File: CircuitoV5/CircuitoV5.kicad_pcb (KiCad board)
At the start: 2 copper layers, 27 x 62 mm, 18 parts, among them J1 Conn_01x05, J2 Screw_Terminal_01x02, J3 Screw_Terminal_01x02, U1 LM324, U2 LM358

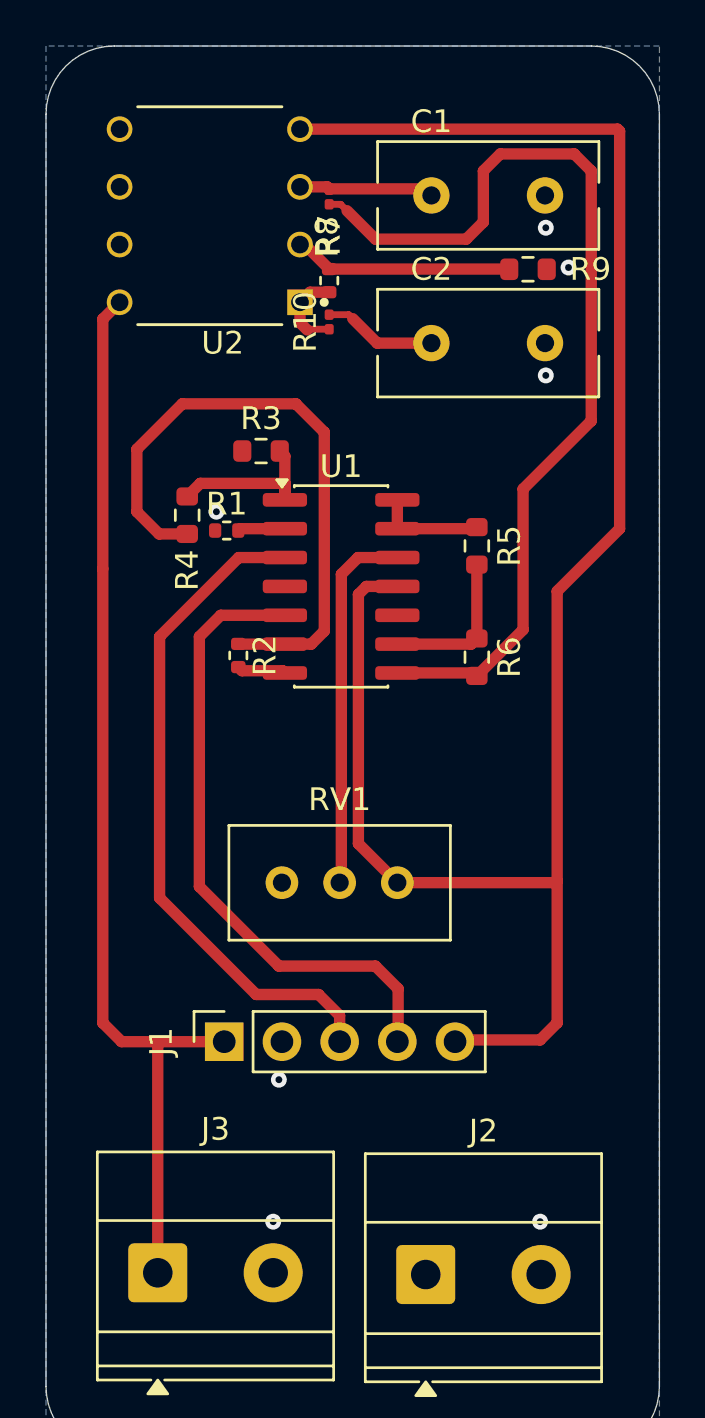
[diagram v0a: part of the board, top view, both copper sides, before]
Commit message: Enrutamiento v2 parcial
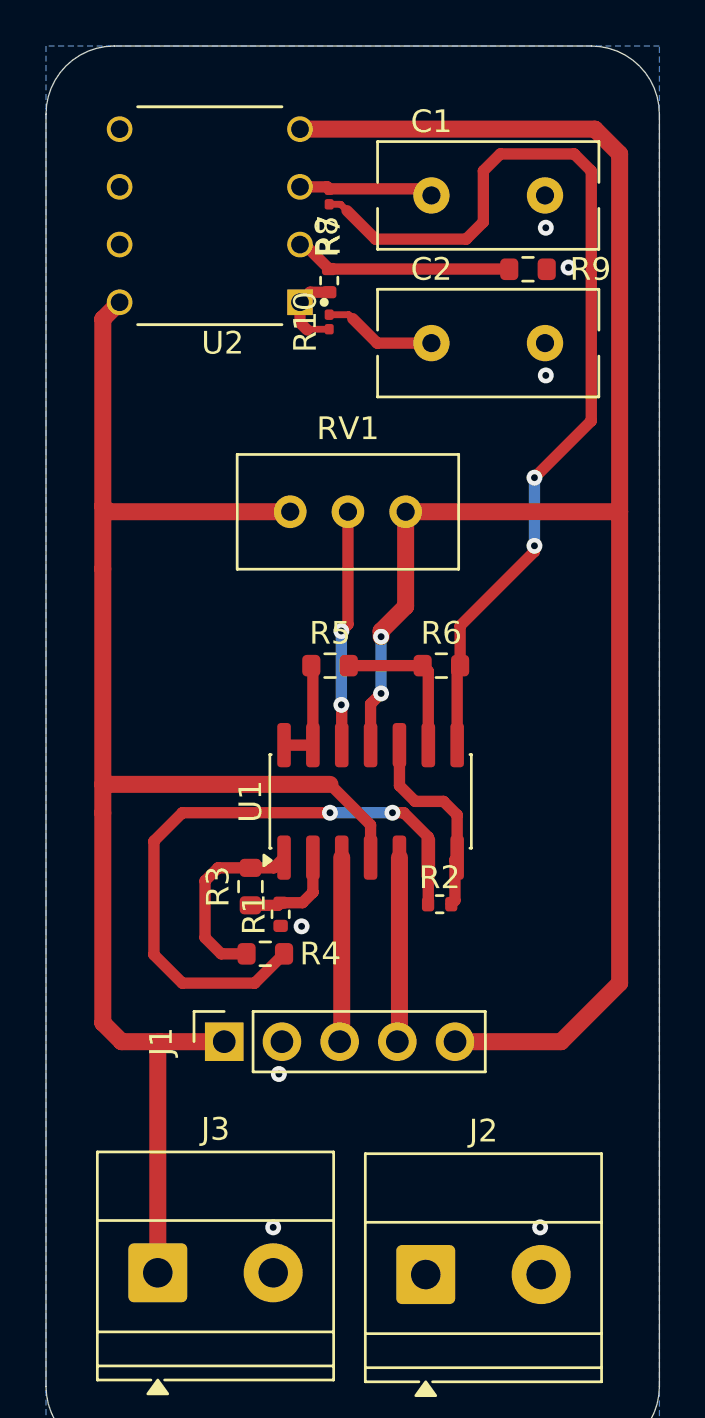
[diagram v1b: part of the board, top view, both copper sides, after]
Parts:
- moved R4 19.6 mm to (49.7, 88.0), turned to 0 degrees
- moved R3 19.2 mm to (49.0, 85.0), turned to 90 degrees
- moved R1 17.1 mm to (50.3, 86.2), turned to 90 degrees
- moved RV1 16.3 mm to (55.8, 68.5)
- moved R2 14.1 mm to (57.3, 85.8), turned to 0 degrees
- moved U1 9.55 mm to (54.3, 81.2), turned to 90 degrees
- moved R5 8.34 mm to (52.5, 75.3), turned to 0 degrees
- moved R6 1.61 mm to (57.4, 75.3), turned to 0 degrees
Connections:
- C2 pad 1: Net-(C2-Pad1) -> /Vout
- R10 pad 2: Net-(C2-Pad1) -> /Vout
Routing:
- net VCC: track 47.9 -> 70.2 mm
- net /Va: track 29.7 -> 8.14 mm
- net /Vb: track 28.1 -> 8.14 mm
- net Net-(U1C-+): track 2.72 -> 8.89 mm
- net Net-(U1D-+): track 16.4 -> 10.4 mm, vias 0 -> 2
- net Net-(C2-Pad1): track 5.02 -> 0.00 mm
- net /Vout: track 0.00 -> 5.02 mm
- net Net-(U1A--): track 2.08 -> 4.51 mm
- net VEE: track 81.7 -> 79.7 mm, vias 0 -> 2
- net Net-(R3-Pad2): track 7.51 -> 8.52 mm
- net Net-(R6-Pad2): track 43.2 -> 43.1 mm, vias 0 -> 2
- net Net-(U1B--): track 27.7 -> 27.8 mm, vias 0 -> 2

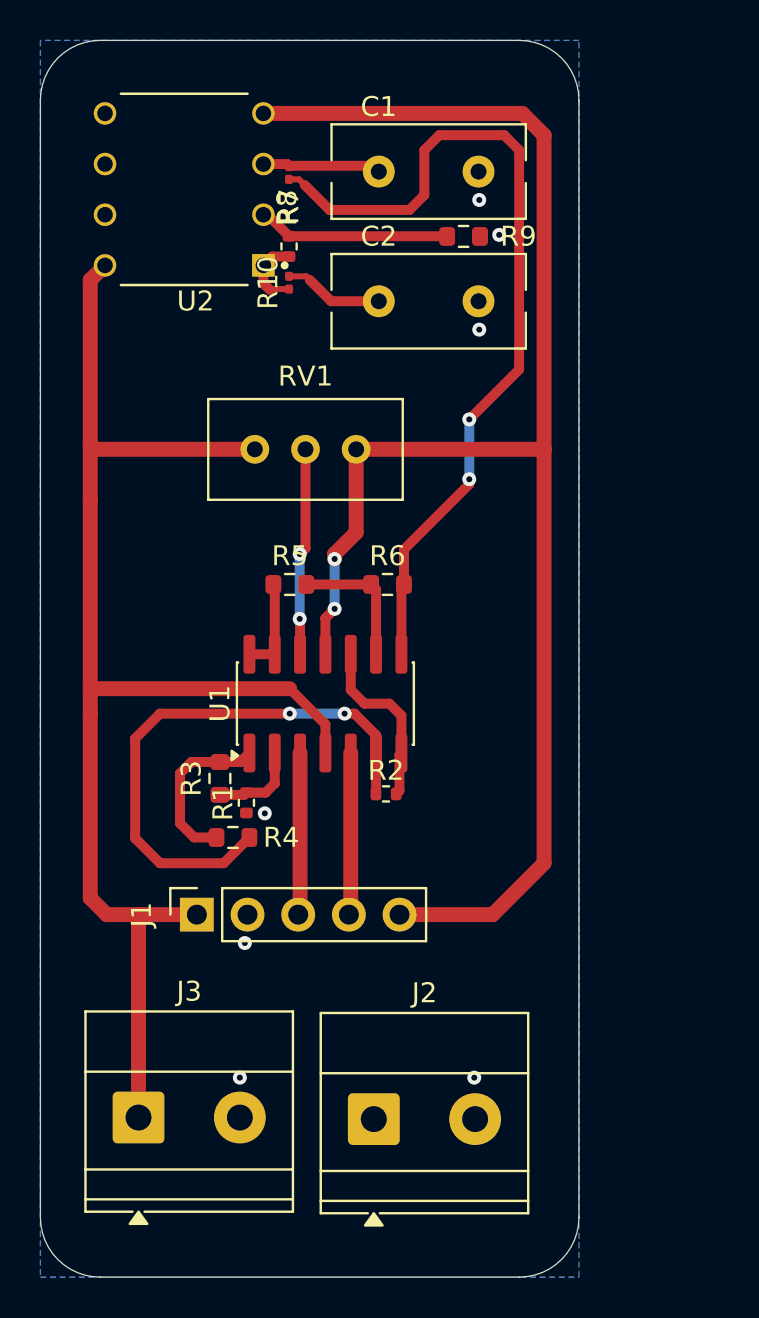
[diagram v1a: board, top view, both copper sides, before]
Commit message: Enrutado completo V3 y errores importantes corregidos, quedan algunos por ignorar
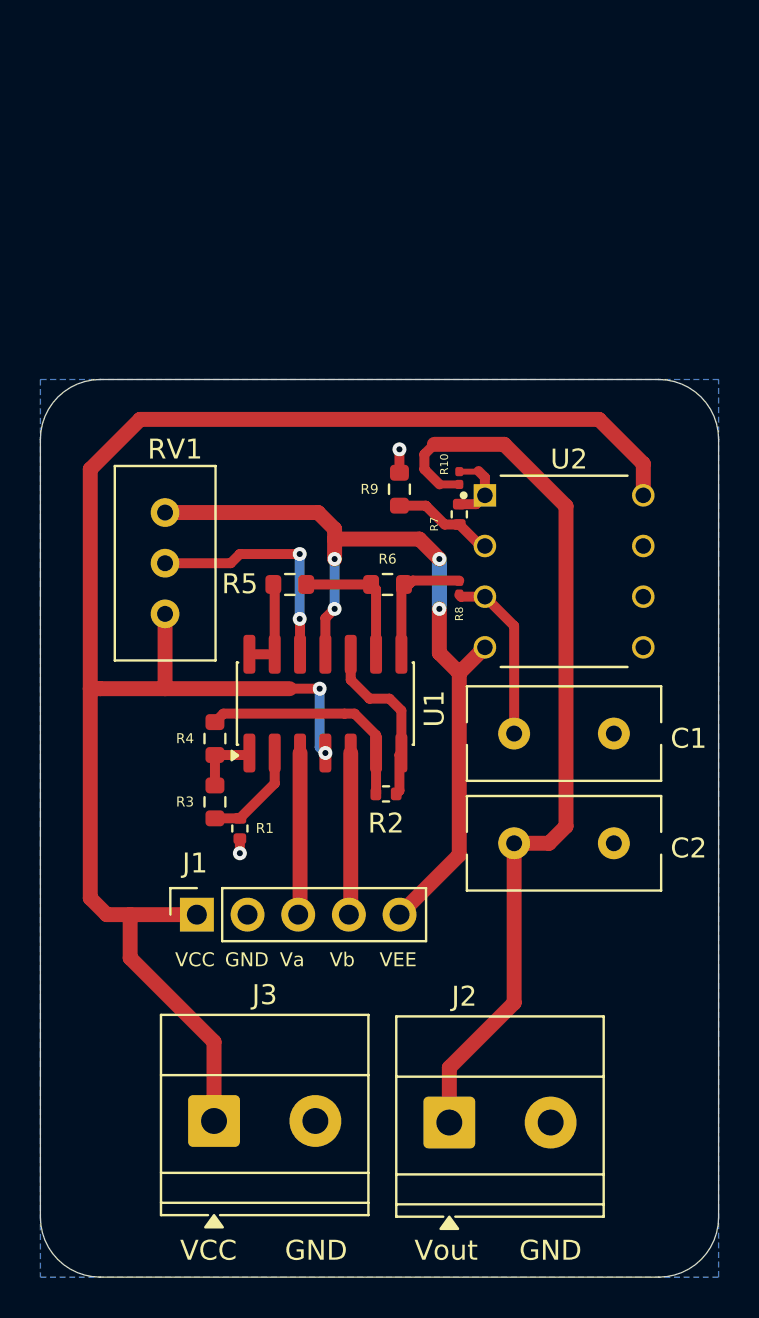
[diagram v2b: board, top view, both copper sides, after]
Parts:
- moved C1 29.0 mm to (62.2, 82.8)
- moved C2 28.0 mm to (62.2, 88.2)
- moved U2 27.0 mm to (66.3, 74.6), turned to 0 degrees
- moved R8 22.5 mm to (61.0, 75.4), turned to 90 degrees
- moved R7 15.9 mm to (61.0, 71.8), turned to 90 degrees
- moved R9 13.1 mm to (58.0, 70.5), turned to -90 degrees
- moved R10 13.0 mm to (61.0, 69.9), turned to -90 degrees
- moved RV1 10.1 mm to (46.2, 71.7), turned to 90 degrees
- moved R4 5.04 mm to (48.8, 83.0), turned to 90 degrees
- moved J2 3.79 mm to (60.5, 102.2)
- moved J3 3.79 mm to (48.7, 102.2)
- moved R1 1.33 mm to (50.0, 87.5)
- moved R3 1.20 mm to (48.8, 86.2)
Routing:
- net /Vout: track 5.02 -> 46.5 mm
- net VEE: track 79.7 -> 42.3 mm, vias 2 -> 4
- net Net-(R6-Pad2): track 43.1 -> 6.41 mm, vias 2 -> 0
- net VCC: track 70.2 -> 89.1 mm, vias 0 -> 2
- net Net-(U1B--): track 27.8 -> 11.7 mm, vias 2 -> 0
- net Net-(R3-Pad2): track 8.52 -> 3.29 mm
- net Net-(U2A--): track 9.66 -> 5.12 mm
- net Net-(U2A-+): track 5.94 -> 8.79 mm
- net GND: track 0.00 -> 2.42 mm, vias 7 -> 2
- net Net-(U1D-+): track 10.4 -> 12.0 mm
- net Net-(U1A--): track 4.51 -> 5.25 mm
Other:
- board size 27 x 62 mm -> 34 x 45 mm
- board text added: "GND"
- board text added: "VCC"
- board text added: "VEE"
- board text added: "Va"
- board text added: "Vb"
- board text added: "Vout"

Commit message: Ultimos retoques de enrutamiento
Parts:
- moved R10 1.77 mm to (62.5, 69.0), turned to 0 degrees
- moved R8 0.61 mm to (60.8, 76.0), turned to 180 degrees
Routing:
- net VEE: track 42.3 -> 69.5 mm, vias 4 -> 0
- net /Vout: track 46.5 -> 40.1 mm
- net Net-(U1D-+): track 12.0 -> 13.8 mm, vias 2 -> 0
- net Net-(U1B--): track 11.7 -> 12.3 mm
- net VCC: track 89.1 -> 89.5 mm, vias 2 -> 0

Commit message: Routed and done
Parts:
- added C3: LM324, Capacitor_THT:C_Disc_D5.0mm_W2.5mm_P2.50mm, F.Cu at (92.9, 77.9)
- added C4: LM324, Capacitor_THT:C_Disc_D5.0mm_W2.5mm_P2.50mm, F.Cu at (92.9, 74.7)
- added C5: LM358, Capacitor_THT:C_Disc_D5.0mm_W2.5mm_P2.50mm, F.Cu at (92.3, 45.6)
- added C6: LM358, Capacitor_THT:C_Disc_D5.0mm_W2.5mm_P2.50mm, F.Cu at (106.7, 48.2)
- J1: footprint Connector_PinSocket_2.54mm:PinSocket_1x05_P2.54mm_Vertical -> Connector_PinSocket_2.54mm:PinSocket_1x05_P2.54mm_Horizontal
- J2, J3: value Screw_Terminal_01x02 -> Conn_01x02; footprint TerminalBlock_Phoenix:TerminalBlock_Phoenix_MKDS-1,5-2-5.08_1x02_P5.08mm_Horizontal -> Connector_PinSocket_2.54mm:PinSocket_1x02_P2.54mm_Vertical
- R1, R2, R7: footprint Resistor_SMD:R_0402_1005Metric -> Resistor_THT:R_Axial_DIN0207_L6.3mm_D2.5mm_P10.16mm_Horizontal
- R10, R8: footprint Resistor_SMD:R_0201_0603Metric -> Resistor_THT:R_Axial_DIN0207_L6.3mm_D2.5mm_P10.16mm_Horizontal
- R3, R4, R5, R6, R9: footprint Resistor_SMD:R_0603_1608Metric -> Resistor_THT:R_Axial_DIN0207_L6.3mm_D2.5mm_P10.16mm_Horizontal
- U1: footprint Package_SO:SOIC-14_3.9x8.7mm_P1.27mm -> Package_DIP:DIP-14_W7.62mm
- U2: footprint footprints:DIP794W45P254L959H508Q8 -> Package_DIP:DIP-8_W7.62mm
- moved J2 77.2 mm to (111.7, 44.5), turned to 90 degrees
- moved J3 69.3 mm to (87.1, 44.5), turned to -90 degrees
- moved C1 50.2 mm to (105.0, 56.5)
- moved R2 49.9 mm to (107.2, 84.5)
- moved R6 47.2 mm to (103.9, 67.5)
- moved J1 46.2 mm to (93.9, 88.8)
- moved R4 46.0 mm to (94.8, 84.5), turned to 0 degrees
- moved R8 45.2 mm to (103.9, 62.5), turned to 0 degrees
- moved U1 43.1 mm to (97.3, 79.8)
- moved R1 42.6 mm to (89.0, 70.5), turned to -90 degrees
- moved R7 42.1 mm to (100.6, 57.5), turned to 180 degrees
- moved R5 38.7 mm to (90.4, 67.5)
- moved RV1 38.2 mm to (84.0, 77.5), turned to -90 degrees
- moved U2 37.9 mm to (95.7, 50.8), turned to 90 degrees
- moved C2 37.5 mm to (85.0, 58.5), turned to -90 degrees
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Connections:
- C2 pad 1: /Vout -> Net-(C2-Pad1)
- J1 pad 2: GND -> /Va
- J1 pad 3: /Va -> /Vb
- J1 pad 4: /Vb -> GND
- R10 pad 1: Net-(R10-Pad1) -> Net-(U2B-+)
- R10 pad 2: /Vout -> Net-(C2-Pad1)
- R7 pad 2: Net-(R10-Pad1) -> Net-(U2B-+)
- U2 pad 1: Net-(R10-Pad1) -> Net-(U2B-+)
- U2 pad 5: unconnected-(U2B-+-Pad5) -> Net-(U2B-+)
- U2 pad 6: unconnected-(U2B---Pad6) -> /Vout
- U2 pad 7: unconnected-(U2-Pad7) -> /Vout
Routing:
- net VEE: track 69.5 -> 127.5 mm
- net /Vout: track 40.1 -> 15.9 mm
- net Net-(U2B-+): track 0.00 -> 20.2 mm
- net Net-(U1A--): track 5.25 -> 21.6 mm
- net VCC: track 89.5 -> 104.6 mm
- net Net-(U1D-+): track 13.8 -> 23.2 mm
- net Net-(C2-Pad1): track 0.00 -> 8.10 mm
- net Net-(U2A-+): track 8.73 -> 16.6 mm
- net Net-(U1C-+): track 8.75 -> 16.5 mm
- net Net-(U2A--): track 5.12 -> 12.7 mm
- net Net-(U1D--): track 4.80 -> 11.4 mm
- net /Vb: track 8.14 -> 13.8 mm
- net Net-(R3-Pad2): track 3.29 -> 8.50 mm
- net Net-(U1C--): track 6.85 -> 11.4 mm
- net Net-(R6-Pad2): track 6.06 -> 10.3 mm
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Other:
- board size 34 x 45 mm -> 43.4 x 59.6 mm
- board text removed: "GND"
- board text removed: "VCC"
- board text removed: "VEE"
- board text removed: "Va"
- board text removed: "Vb"
- board text removed: "Vout"

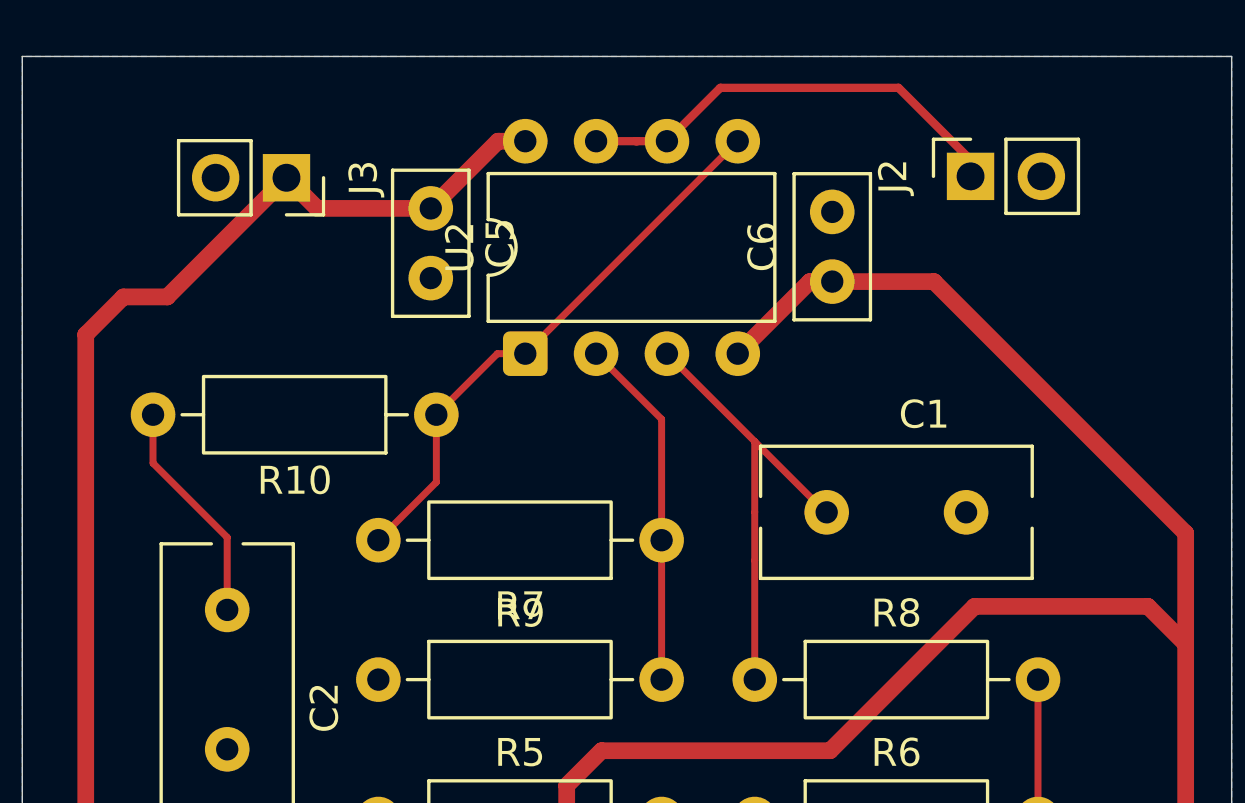
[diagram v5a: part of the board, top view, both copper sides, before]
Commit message: Añadidos tag en silkscreen para pines de conexion
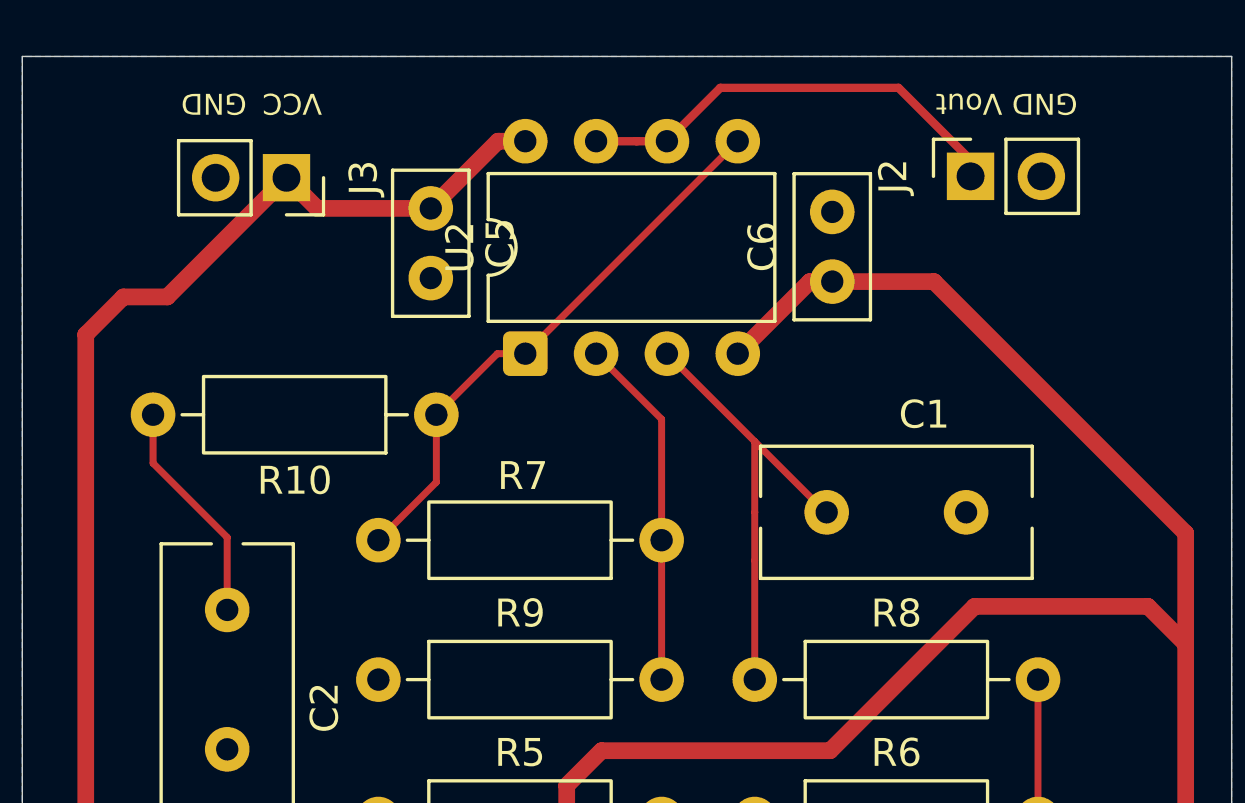
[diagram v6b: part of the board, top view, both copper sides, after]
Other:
- board text added: "A"
- board text added: "B"
- board text added: "GND"
- board text added: "VCC"
- board text added: "VEE"
- board text added: "Vout"
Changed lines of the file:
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@@
 		(tags "Resistor Axial_DIN0207 series Axial Horizontal pin pitch 10.16mm 0.25W = 1/4W length 6.3mm diameter 2.5mm")
 		(property "Reference" "R7"
-			(at 5.08 -2.37 0)
+			(at 4.98 2.3 0)
 			(layer "F.SilkS")
 			(effects
@@
 		(layer "Edge.Cuts")
 	)
+	(gr_text "GND"
+		(at 85.7 41.4 180)
+		(layer "F.SilkS")
+		(effects
+			(font
+				(size 0.75 0.75)
+				(thickness 0.1)
+			)
+			(justify left bottom)
+		)
+	)
+	(gr_text "VCC"
+		(at 88.4 41.4 180)
+		(layer "F.SilkS")
+		(effects
+			(font
+				(size 0.75 0.75)
+				(thickness 0.1)
+			)
+			(justify left bottom)
+		)
+	)
+	(gr_text "Vout"
+		(at 112.8 41.4 180)
+		(layer "F.SilkS")
+		(effects
+			(font
+				(size 0.75 0.75)
+				(thickness 0.1)
+			)
+			(justify left bottom)
+		)
+	)
+	(gr_text "GND"
+		(at 115.5 41.4 180)
+		(layer "F.SilkS")
+		(effects
+			(font
+				(size 0.75 0.75)
+				(thickness 0.1)
+			)
+			(justify left bottom)
+		)
+	)
+	(gr_text "VCC"
+		(at 95.1 98.4 0)
+		(layer "B.SilkS")
+		(effects
+			(font
+				(size 0.75 0.75)
+				(thickness 0.1)
+			)
+			(justify left bottom mirror)
+		)
+	)
+	(gr_text "A"
+		(at 96.8 98.4 0)
+		(layer "B.SilkS")
+		(effects
+			(font
+				(size 0.75 0.75)
+				(thickness 0.1)
+			)
+			(justify left bottom mirror)
+		)
+	)
+	(gr_text "B"
+		(at 99.4 98.4 0)
+		(layer "B.SilkS")
+		(effects
+			(font
+				(size 0.75 0.75)
+				(thickness 0.1)
+			)
+			(justify left bottom mirror)
+		)
+	)
+	(gr_text "GND"
+		(at 102.7 98.4 0)
+		(layer "B.SilkS")
+		(effects
+			(font
+				(size 0.75 0.75)
+				(thickness 0.1)
+			)
+			(justify left bottom mirror)
+		)
+	)
+	(gr_text "VEE"
+		(at 105.1 98.4 0)
+		(layer "B.SilkS")
+		(effects
+			(font
+				(size 0.75 0.75)
+				(thickness 0.1)
+			)
+			(justify left bottom mirror)
+		)
+	)
 	(point
